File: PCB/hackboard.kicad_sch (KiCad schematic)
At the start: 160 parts, among them SW1 SW_Push, SW10 SW_Push, SW11 SW_Push, SW12 SW_Push, SW13 SW_Push, SW14 SW_Push, SW15 SW_Push, SW16 SW_Push, SW17 SW_Push, SW18 SW_Push, SW19 SW_Push, SW2 SW_Push, SW20 SW_Push, SW21 SW_Push, SW22 SW_Push, SW23 SW_Push, SW24 SW_Push, SW25 SW_Push, SW26 SW_Push, SW27 SW_Push, SW28 SW_Push, SW29 SW_Push, SW3 SW_Push, SW30 SW_Push, SW31 SW_Push, SW32 SW_Push, SW33 SW_Push, SW34 SW_Push, SW35 SW_Push, SW36 SW_Push, SW37 SW_Push, SW38 SW_Push, SW39 SW_Push, SW4 SW_Push, SW40 SW_Push, SW41 SW_Push, SW42 SW_Push, SW43 SW_Push, SW44 SW_Push, SW45 SW_Push, SW46 SW_Push, SW47 SW_Push, SW48 SW_Push, SW49 SW_Push, SW5 SW_Push, SW50 SW_Push, SW51 SW_Push, SW52 SW_Push, SW53 SW_Push, SW54 SW_Push, SW55 SW_Push, SW56 SW_Push, SW57 SW_Push, SW58 SW_Push, SW59 SW_Push, SW6 SW_Push, SW60 SW_Push, SW61 SW_Push, SW62 SW_Push, SW63 SW_Push, SW64 SW_Push, SW65 SW_Push, SW66 SW_Push, SW67 SW_Push, SW68 SW_Push, SW69 SW_Push, SW7 SW_Push, SW70 SW_Push, SW71 SW_Push, SW72 SW_Push, SW73 SW_Push, SW74 SW_Push, SW75 SW_Push, SW76 SW_Push, SW77 SW_Push, SW78 SW_Push, SW79 RotaryEncoder_Switch, SW8 SW_Push, SW9 SW_Push, U1 Pico

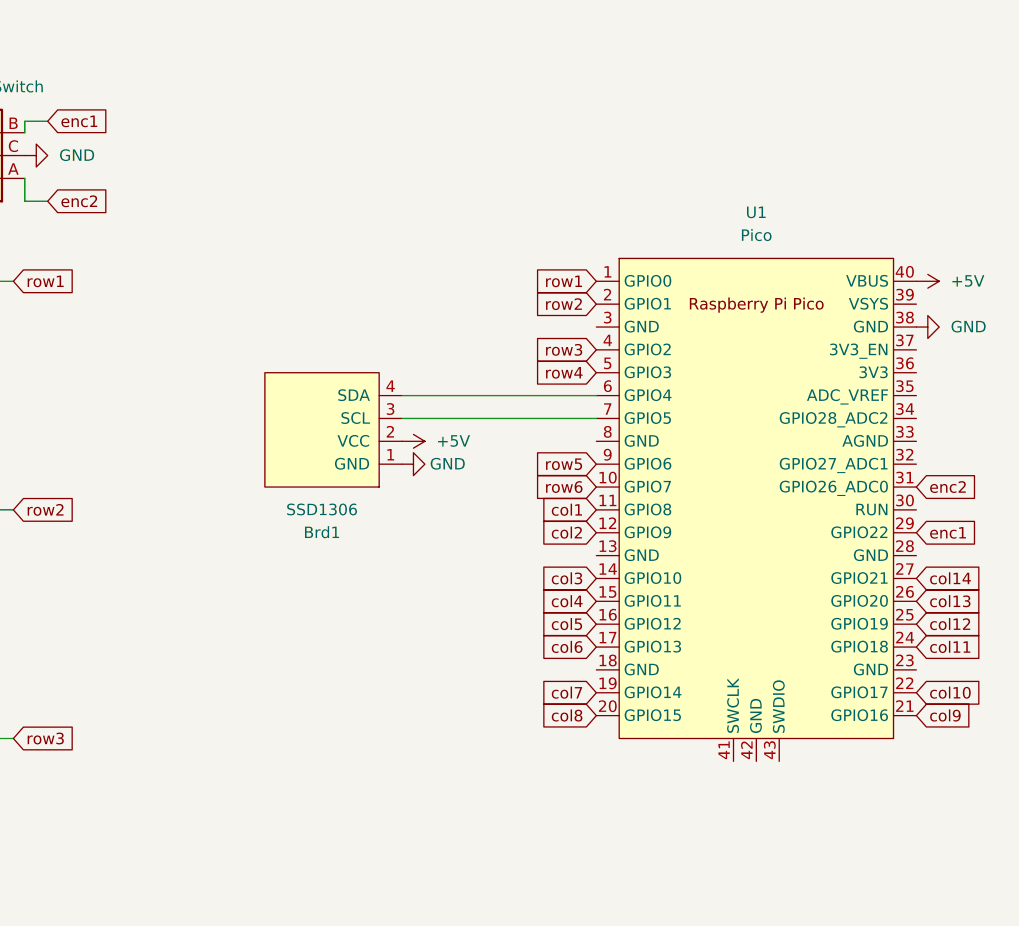
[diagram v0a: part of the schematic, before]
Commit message: split case into 2, recompile STL and STEP files
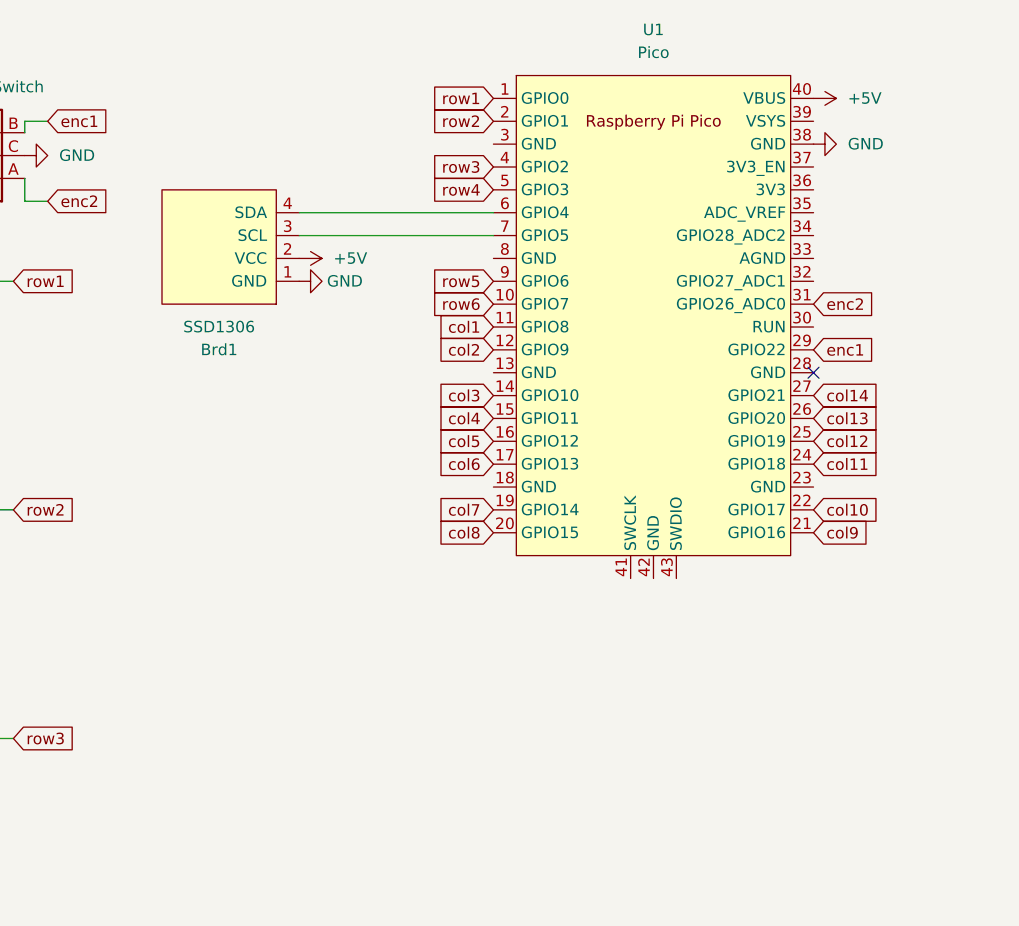
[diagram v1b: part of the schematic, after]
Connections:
- no-connect marks 0 -> 1
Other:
- moved on the sheet: Brd1, U1
